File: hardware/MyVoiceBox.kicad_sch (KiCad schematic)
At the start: 25 parts, among them J1 USB_B_Micro, J2 Gain Select, J3 AudioJack3, SW1 BOOT, SW2 RESET, U2 HT7833, U3 INMP441, U4 INMP441, U6 Debug Serial Port, U7 HT7833

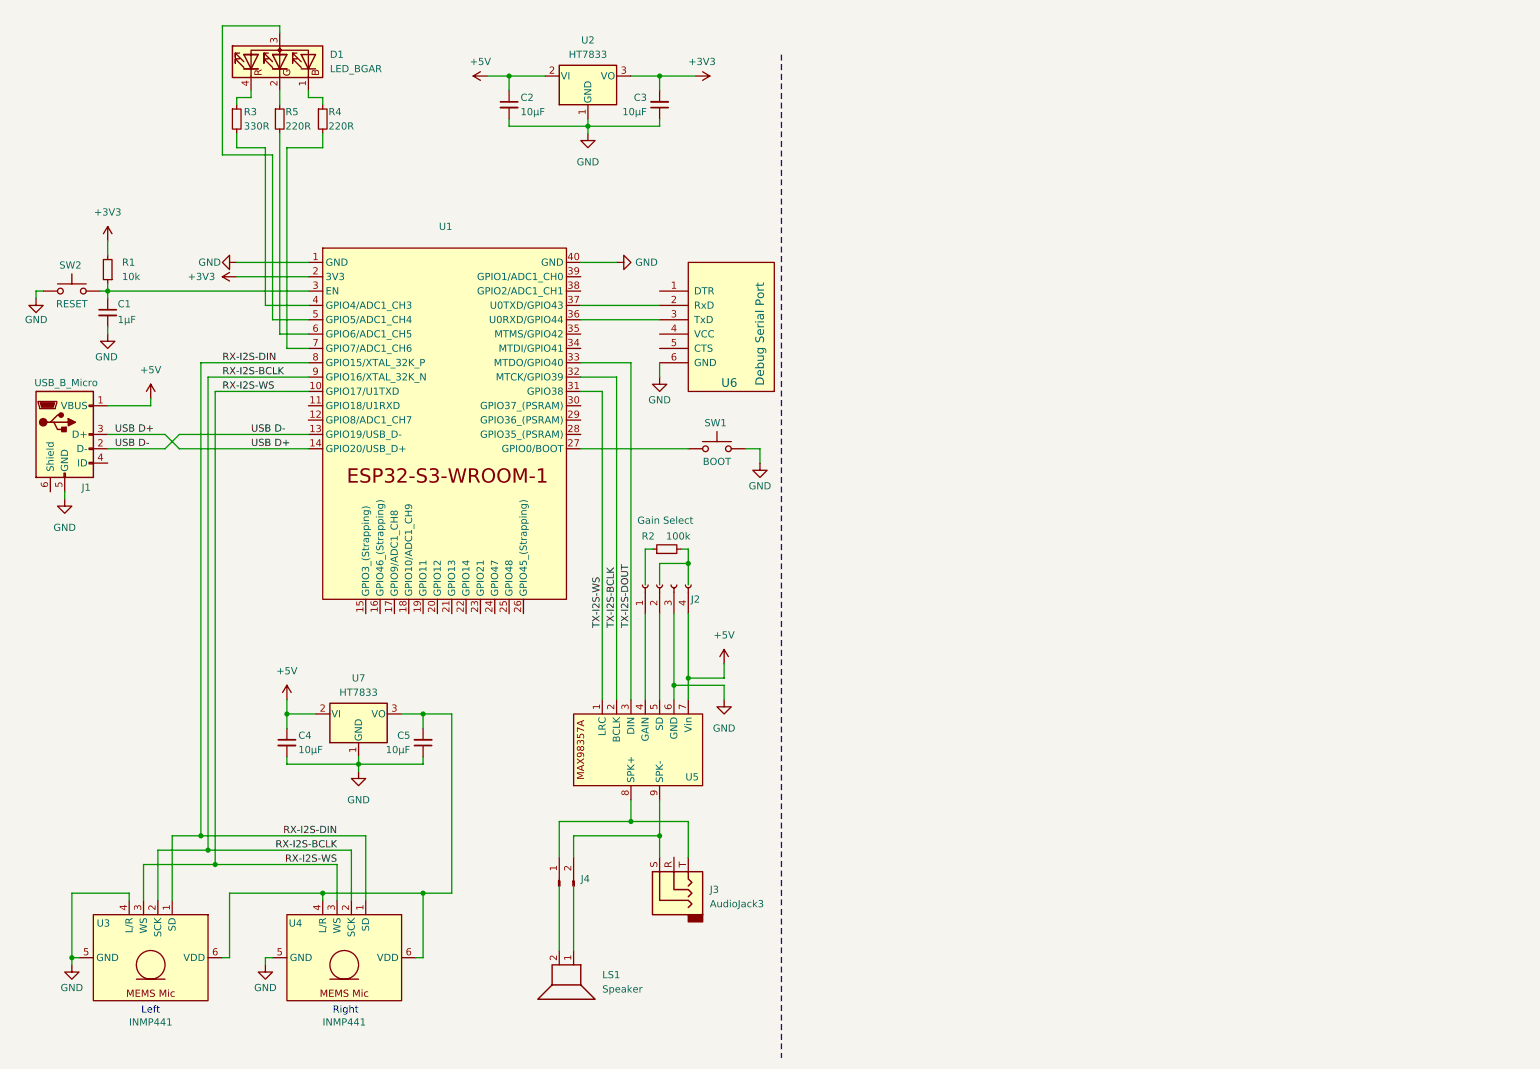
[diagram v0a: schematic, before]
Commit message: major refactoring, added support for climate sensor and display
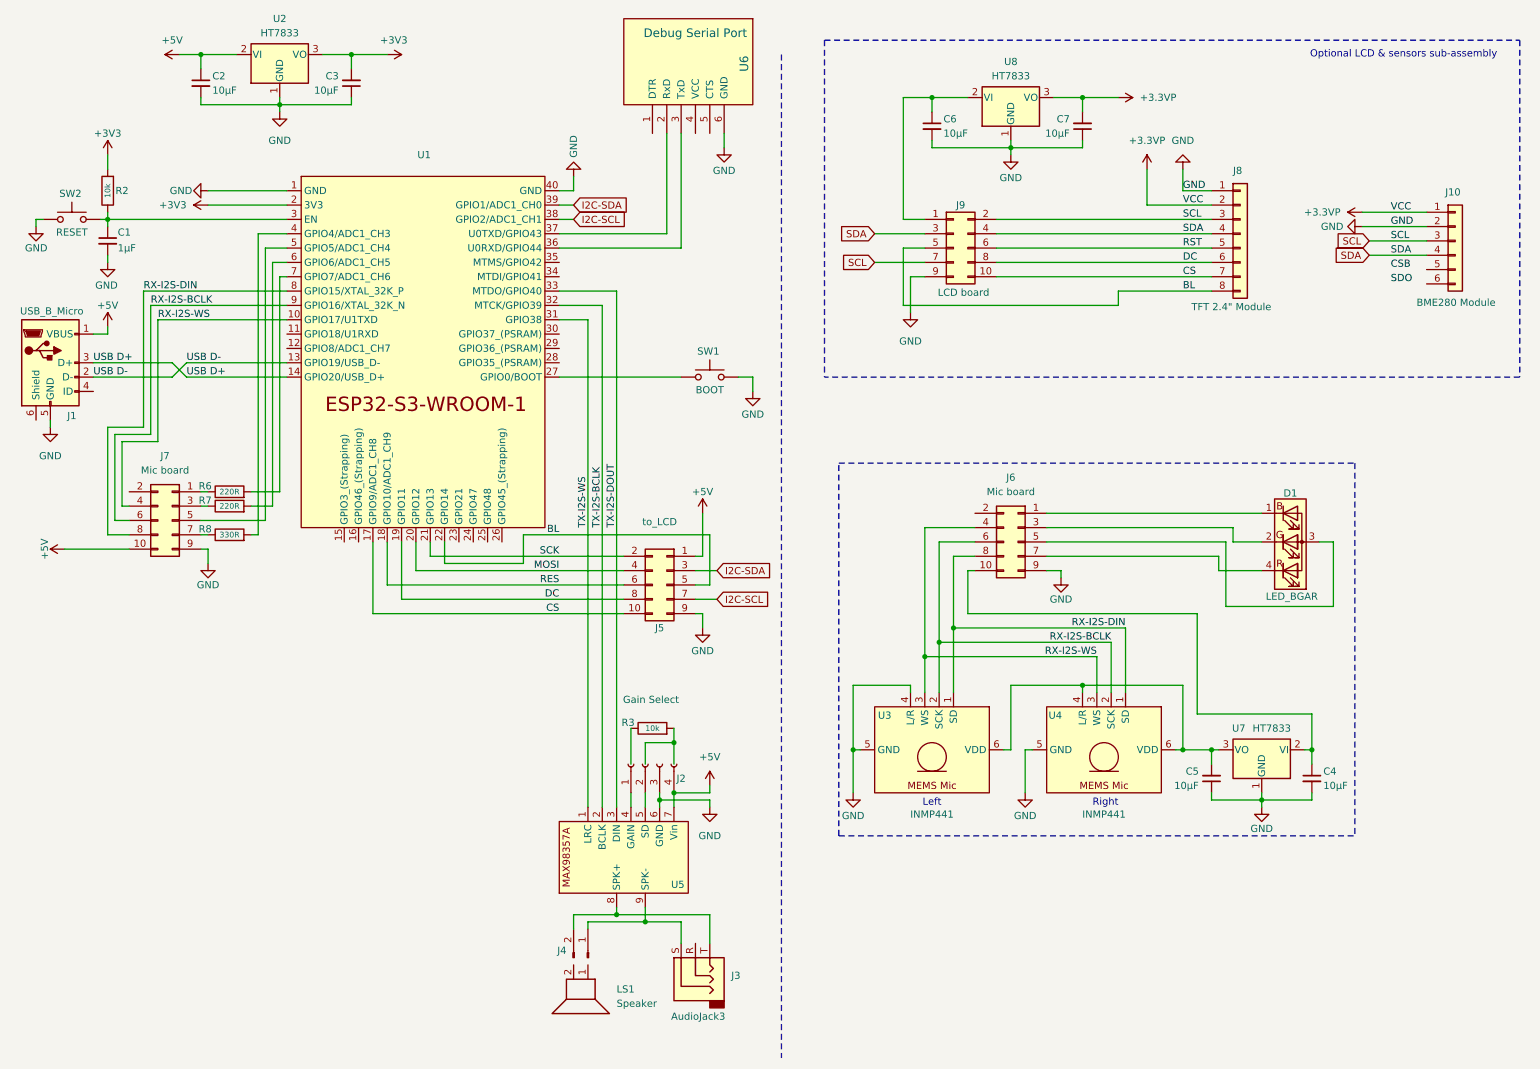
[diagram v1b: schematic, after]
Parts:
- removed R1: 10k, symbol Device:R_Small
- removed R2: 100k, symbol Device:R_Small
- removed R3: 330R, symbol Device:R_Small
- removed R4, R5: 220R, symbol Device:R_Small
- added C6, C7: 10µF, symbol Device:C_Small
- added J10: BME280 Module, symbol Connector_Generic:Conn_01x06
- added J5: to_LCD, symbol Connector_Generic:Conn_02x05_Odd_Even
- added J6, J7: Mic board, symbol Connector_Generic:Conn_02x05_Odd_Even
- added J8: TFT 2.4" Module, symbol Connector_Generic:Conn_01x08
- added J9: LCD board, symbol Connector_Generic:Conn_02x05_Odd_Even
- added R2, R3: 10k, symbol Device:R
- added R6, R7: 220R, symbol Device:R
- added R8: 330R, symbol Device:R
- added U8: HT7833, Package_TO_SOT_THT:TO-92_Inline, symbol Regulator_Linear:MCP1700x-500xxTO
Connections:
- net +3V3: now also R2.2
- net +5V: now also J5.1 (Pin_1), J7.10 (Pin_10); no longer C4.1, U7.2 (VI)
- net GND: now also C6.2, C7.1, J10.2 (Pin_2), J5.9 (Pin_9), J6.9 (Pin_9), J7.9 (Pin_9), J8.1 (Pin_1), J9.9 (Pin_9), U8.1 (GND)
- net RX-I2S-BCLK: now also J6.6 (Pin_6), J7.6 (Pin_6)
- net RX-I2S-DIN: now also J6.8 (Pin_8), J7.8 (Pin_8)
- net RX-I2S-WS: now also J6.4 (Pin_4), J7.4 (Pin_4)
- net at J3.S, U5.9 (SPK-): now also J4.1 (Pin_1); no longer J4.2 (Pin_2)
- net at J3.T, U5.8 (SPK+): now also J4.2 (Pin_2); no longer J4.1 (Pin_1)
- net at D1.4 (RK): now also J6.7 (Pin_7)
- net at U1.4 (GPIO4/ADC1_CH3): now also R8.2
- net at C1.1, SW2.2, U1.3 (EN): now also R2.1
- net at D1.1 (BK): now also J6.1 (Pin_1)
- net at D1.2 (GK): now also J6.3 (Pin_3)
- net at D1.3 (A): now also J6.5 (Pin_5); no longer U1.5 (GPIO5/ADC1_CH4)
- net at U1.6 (GPIO6/ADC1_CH5): now also R7.2
- net at U1.7 (GPIO7/ADC1_CH6): now also R6.2
- net CS: now reaches U1.17 (GPIO9/ADC1_CH8)
- net CS: now also J5.10 (Pin_10), J8.7 (Pin_7), J9.10 (Pin_10)
- net RES: now reaches U1.18 (GPIO10/ADC1_CH9)
- net RES: now also J5.6 (Pin_6)
- net DC: now reaches U1.19 (GPIO11)
- net DC: now also J5.8 (Pin_8), J8.6 (Pin_6), J9.8 (Pin_8)
- net MOSI: now reaches U1.20 (GPIO12)
- net MOSI: now also J5.4 (Pin_4)
- net SCK: now reaches U1.21 (GPIO13)
- net SCK: now also J5.2 (Pin_2)
- net BL: now reaches U1.22 (GPIO14)
- net BL: now also J5.5 (Pin_5), J8.8 (Pin_8), J9.5 (Pin_5)
- net I2C-SCL: now reaches U1.38 (GPIO2/ADC1_CH1)
- net I2C-SCL: now also J5.7 (Pin_7)
- net I2C-SDA: now reaches U1.39 (GPIO1/ADC1_CH0)
- net I2C-SDA: now also J5.3 (Pin_3)
- new net: C4.1, J6.10 (Pin_10), U7.2 (VI)
- new net: J7.1 (Pin_1), R6.1
- new net: J7.7 (Pin_7), R8.1
- new net: C6.1, J9.1 (Pin_1), U8.2 (VI)
- new net: J7.3 (Pin_3), R7.1
- new net: J7.5 (Pin_5), U1.5 (GPIO5/ADC1_CH4)
- new net +3.3VP: C7.2, J10.1 (Pin_1), J8.2 (Pin_2), U8.3 (VO)
- new net RST: J8.5 (Pin_5), J9.6 (Pin_6)
- new net SCL: J10.3 (Pin_3), J8.3 (Pin_3), J9.2 (Pin_2), J9.7 (Pin_7)
- new net SDA: J10.4 (Pin_4), J8.4 (Pin_4), J9.3 (Pin_3), J9.4 (Pin_4)
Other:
- note added: "Optional LCD & sensors sub-assembly"
- moved on the sheet: C1, C2, C3, C4, C5, D1, J1, J2, J3, J4, LS1, SW1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
